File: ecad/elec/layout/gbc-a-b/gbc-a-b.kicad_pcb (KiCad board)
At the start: 2 copper layers, 5 parts

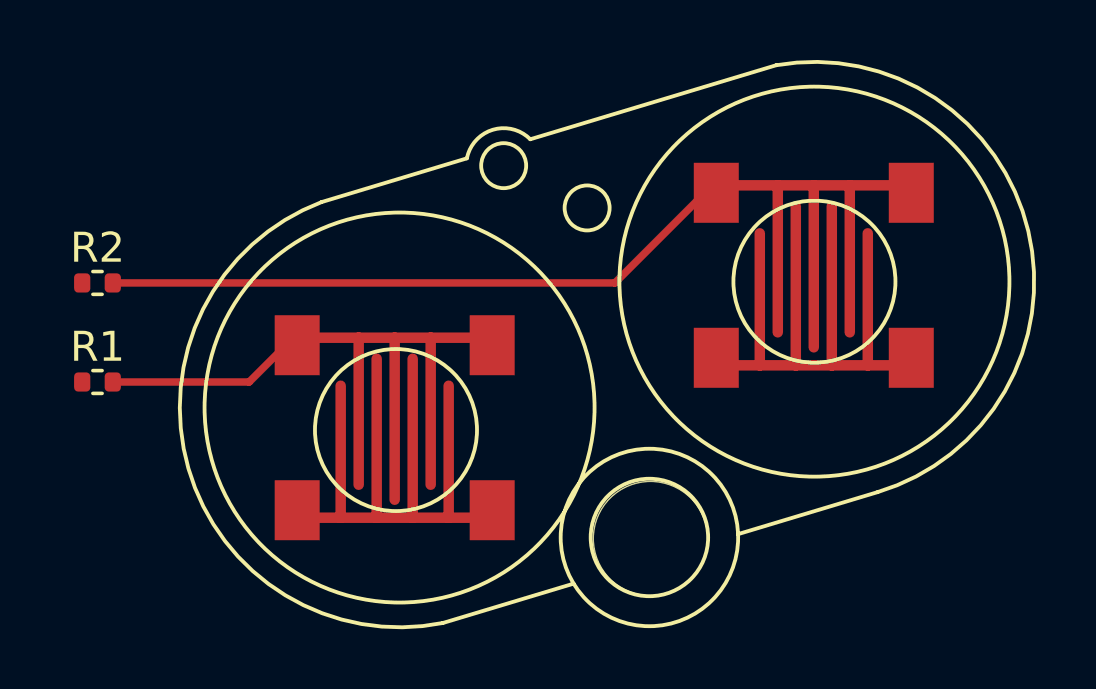
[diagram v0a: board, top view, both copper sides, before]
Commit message: update layouts to use latest footprints and fixed volume buttons and include address pins
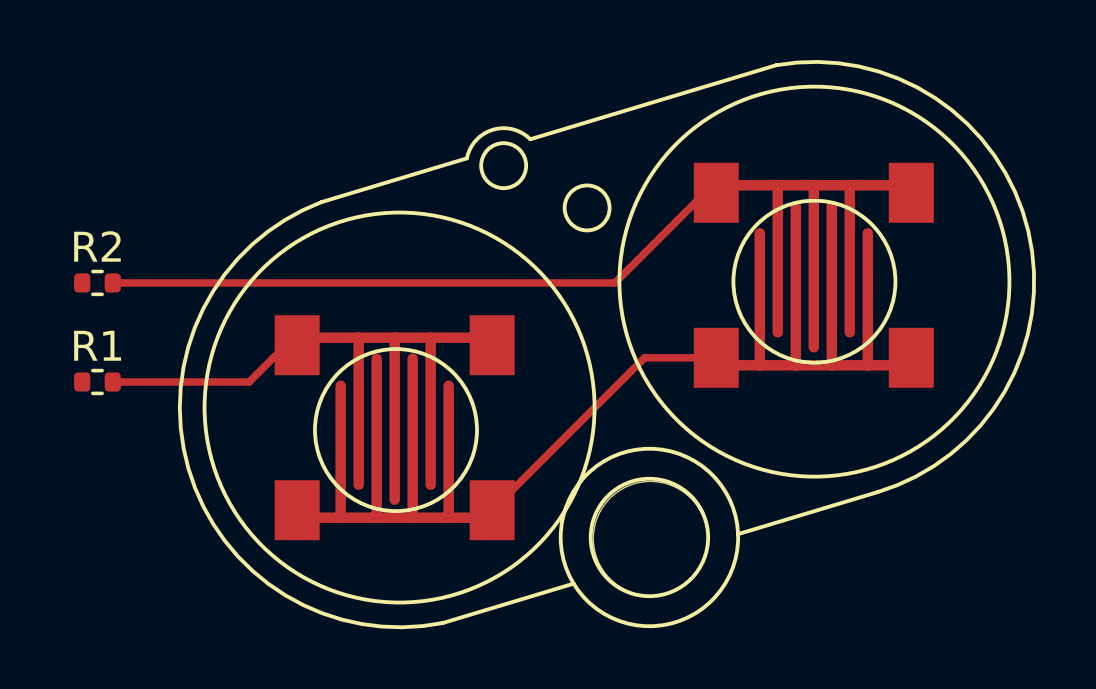
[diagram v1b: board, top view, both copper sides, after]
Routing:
- net vcc: track 0.00 -> 9.57 mm
